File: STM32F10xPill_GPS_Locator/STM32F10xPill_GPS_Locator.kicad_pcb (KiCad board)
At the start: 2 copper layers, 3 parts, among them U1 STM32F100C4Tx, U2 QMC5883P, U4 ATGM336H-5N31

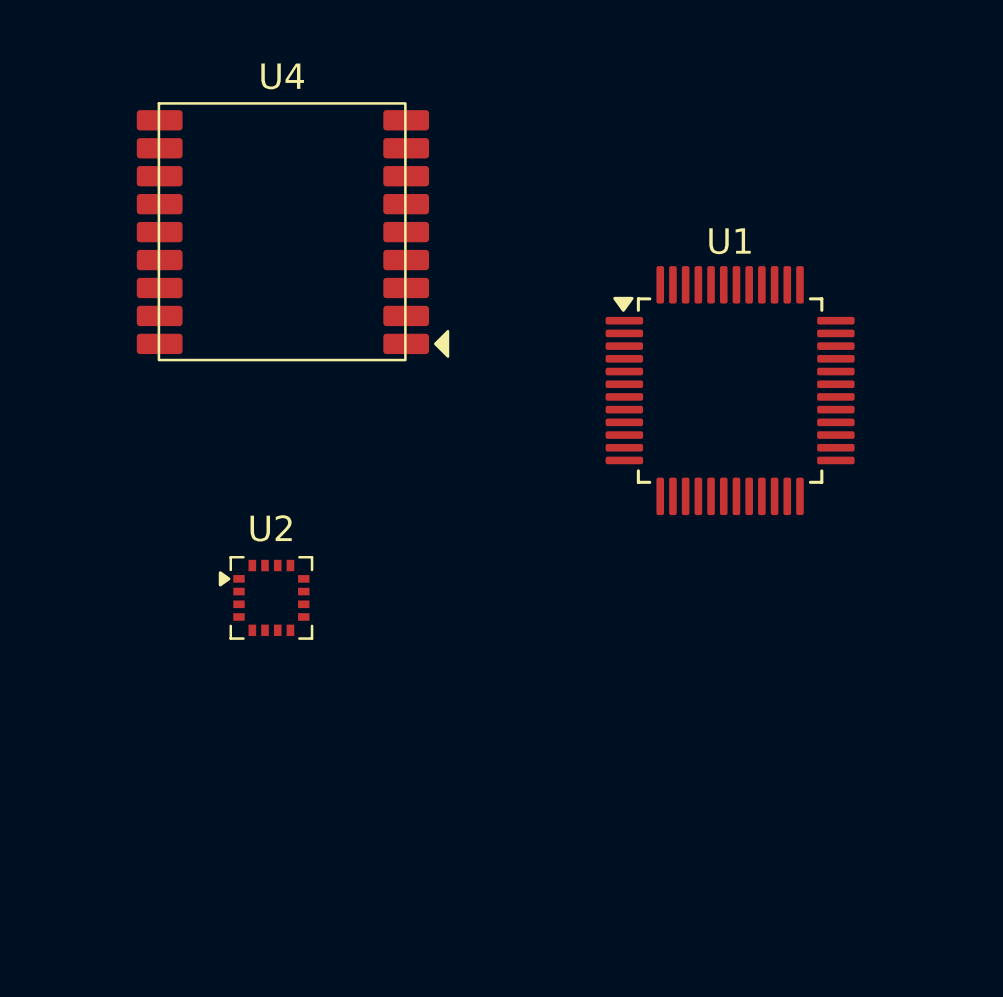
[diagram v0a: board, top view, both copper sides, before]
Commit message: Schematic is largely complete
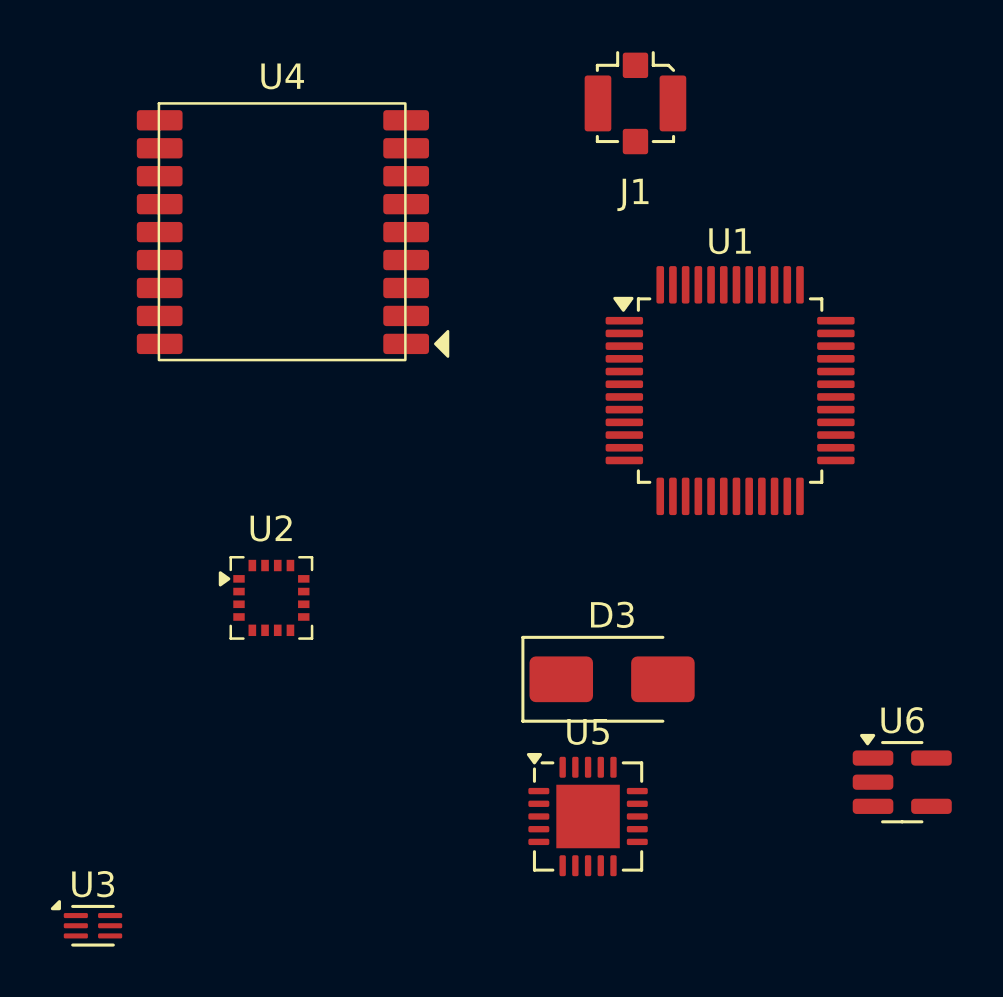
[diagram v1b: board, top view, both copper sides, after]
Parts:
- added D3: SMAJ5.0A, Diode_SMD:D_SMA, F.Cu at (143.6, 98.2)
- added J1: Antenna, Connector_Coaxial:U.FL_Molex_MCRF_73412-0110_Vertical, F.Cu at (144.5, 75.5)
- added U3: AT2659, Package_DFN_QFN:DFN-6_1.6x1.3mm_P0.4mm, F.Cu at (123.2, 107.9)
- added U5: MCP73871T-2CCI/ML, Package_DFN_QFN:QFN-20-1EP_4x4mm_P0.5mm_EP2.5x2.5mm, F.Cu at (142.7, 103.6)
- added U6: TPS61022, Package_TO_SOT_SMD:SC-74A-5_1.55x2.9mm_P0.95mm, F.Cu at (155.0, 102.2)
- U1: value STM32F100C4Tx -> STM32F100C4T6
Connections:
- net +3.3V renamed Net-(JP6-B)
- net +BATT renamed Net-(JP7-B)
- U1 pad 21: unconnected-(U1-PB10-Pad21) -> SCK
- U1 pad 22: unconnected-(U1-PB11-Pad22) -> SDA
- U2 pad 1: unconnected-(U2-SCK-Pad1) -> SCK
- U2 pad 10: unconnected-(U2-C1-Pad10) -> Net-(U2-C1)
- U2 pad 11: unconnected-(U2-GND-Pad11) -> GND
- U2 pad 16: unconnected-(U2-SDA-Pad16) -> SDA
- U2 pad 2: unconnected-(U2-VDD-Pad2) -> Net-(JP5-B)
- U2 pad 9: unconnected-(U2-GND-Pad9) -> GND
- U4 pad 1: unconnected-(U4-GND-Pad1) -> GND
- U4 pad 10: unconnected-(U4-GND-Pad10) -> GND
- U4 pad 11: unconnected-(U4-RF_IN-Pad11) -> Net-(U3-RFOUT)
- U4 pad 12: unconnected-(U4-GND-Pad12) -> GND
- U4 pad 16: unconnected-(U4-SDA-Pad16) -> Net-(U4-SDA)
- U4 pad 17: unconnected-(U4-SCL-Pad17) -> Net-(U4-SCL)
- U4 pad 2: unconnected-(U4-TXD-Pad2) -> GPS_TX
- U4 pad 3: unconnected-(U4-ON/OFF-Pad3) -> GPS_RX
- U4 pad 4: unconnected-(U4-1PPS-Pad4) -> Net-(U4-1PPS)
- U4 pad 6: unconnected-(U4-VBAT-Pad6) -> Net-(JP3-B)
- U4 pad 8: unconnected-(U4-VCC-Pad8) -> Net-(JP4-B)
- U4 pad 9: unconnected-(U4-nRESET-Pad9) -> Net-(U4-nRESET)

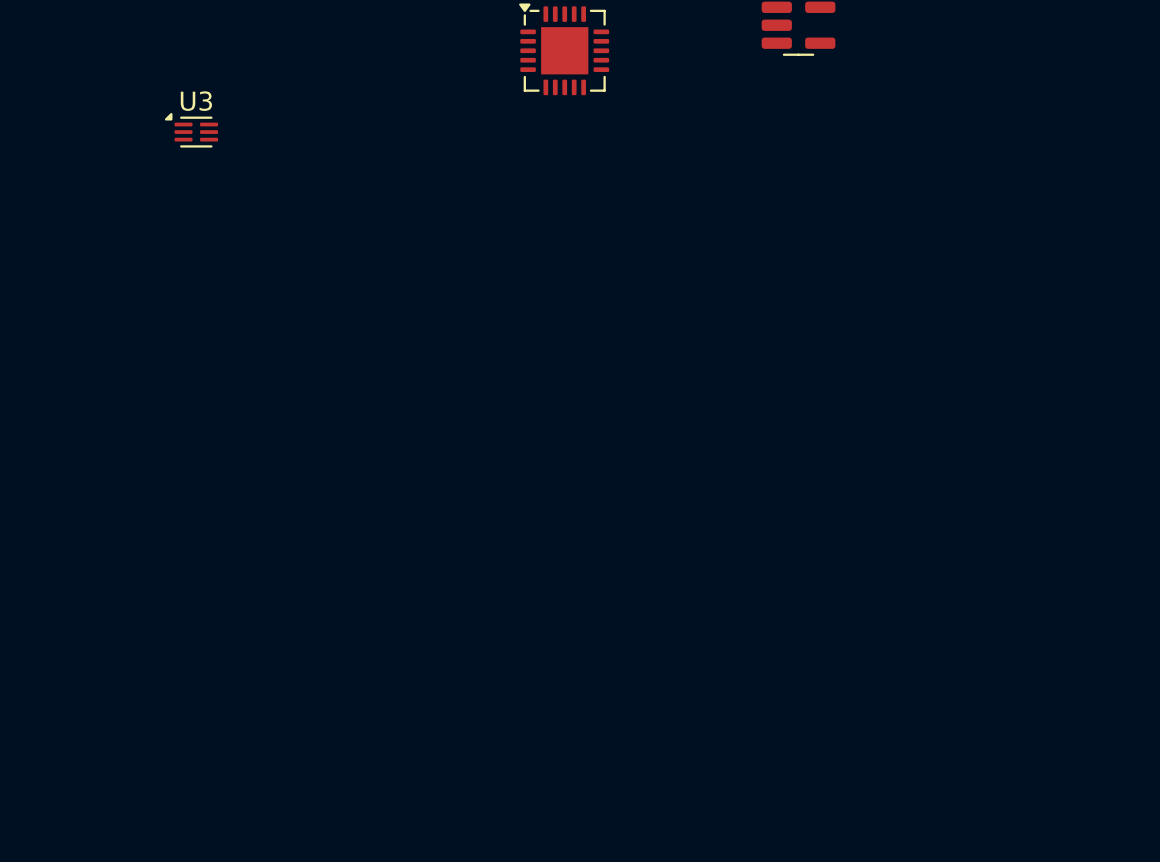
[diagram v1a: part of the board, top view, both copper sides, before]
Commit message: Updated net names, submit schematic for feedback
After feedback is incorporated, PCB layout is ready to begin
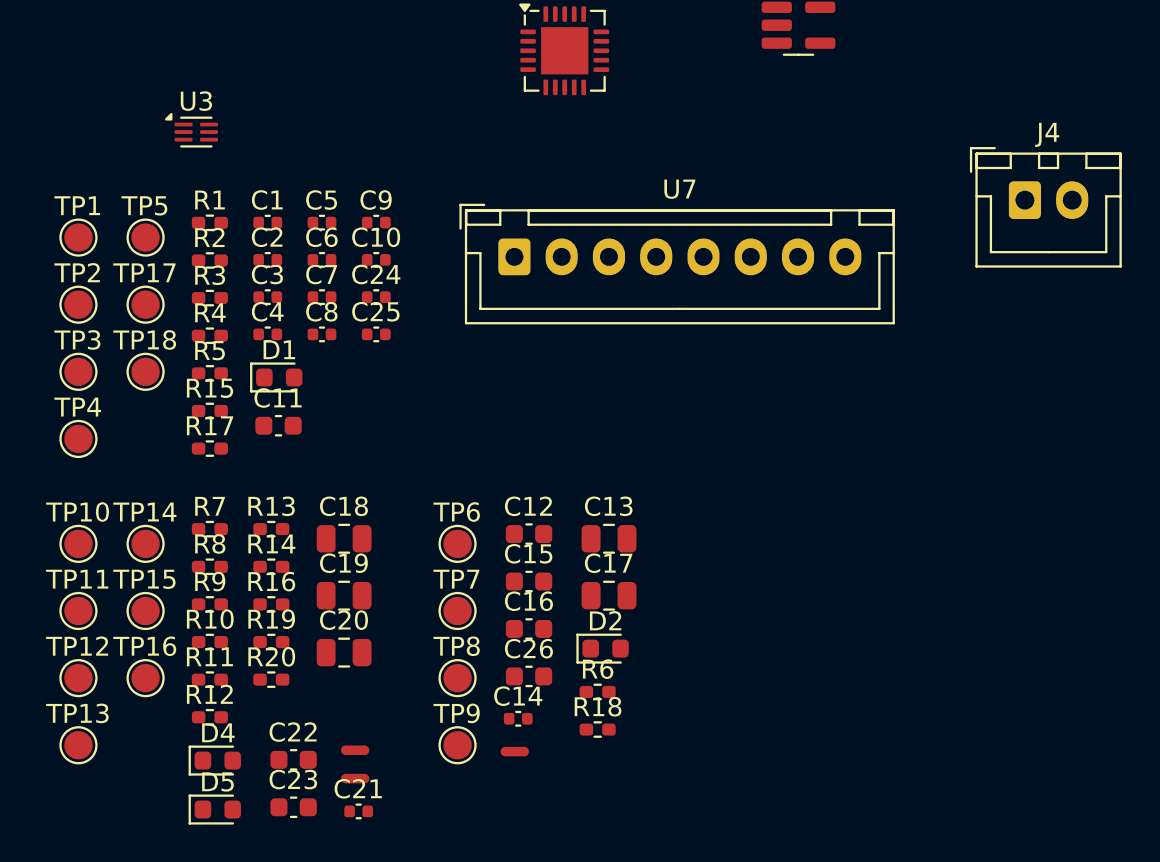
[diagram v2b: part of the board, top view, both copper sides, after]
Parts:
- added C1: 22p, Capacitor_SMD:C_0402_1005Metric, F.Cu at (127.0, 112.7)
- added C10: 22p, Capacitor_SMD:C_0402_1005Metric, F.Cu at (132.7, 114.7)
- added C11: 100n, Capacitor_SMD:C_0603_1608Metric, F.Cu at (127.5, 123.4)
- added C12: 100n, Capacitor_SMD:C_0603_1608Metric, F.Cu at (140.8, 129.2)
- added C13: 4u7, Capacitor_SMD:C_0805_2012Metric, F.Cu at (145.0, 129.4)
- added C14: 470p, Capacitor_SMD:C_0402_1005Metric, F.Cu at (140.2, 138.9)
- added C15: 100n, Capacitor_SMD:C_0603_1608Metric, F.Cu at (140.8, 131.7)
- added C16: 100n, Capacitor_SMD:C_0603_1608Metric, F.Cu at (140.8, 134.2)
- added C17: 10u, Capacitor_SMD:C_0805_2012Metric, F.Cu at (145.0, 132.4)
- added C18: 4u7, Capacitor_SMD:C_0805_2012Metric, F.Cu at (131.0, 129.4)
- added C19: 10u, Capacitor_SMD:C_0805_2012Metric, F.Cu at (131.0, 132.4)
- added C2: 22p, Capacitor_SMD:C_0402_1005Metric, F.Cu at (127.0, 114.7)
- added C20: 2u2, Capacitor_SMD:C_0805_2012Metric, F.Cu at (131.0, 135.4)
- added C21: 1p, Capacitor_SMD:C_0402_1005Metric, F.Cu at (131.8, 143.8)
- added C22: 2u2, Capacitor_SMD:C_0603_1608Metric, F.Cu at (128.3, 141.1)
- added C23: 2u2, Capacitor_SMD:C_0603_1608Metric, F.Cu at (128.3, 143.6)
- added C24: 22p, Capacitor_SMD:C_0402_1005Metric, F.Cu at (132.7, 116.6)
- added C25: 22p, Capacitor_SMD:C_0402_1005Metric, F.Cu at (132.7, 118.6)
- added C26: 100n, Capacitor_SMD:C_0603_1608Metric, F.Cu at (140.8, 136.7)
- added C3: 14p, Capacitor_SMD:C_0402_1005Metric, F.Cu at (127.0, 116.6)
- added C4: 14p, Capacitor_SMD:C_0402_1005Metric, F.Cu at (127.0, 118.6)
- added C5: 100n, Capacitor_SMD:C_0402_1005Metric, F.Cu at (129.8, 112.7)
- added C6: 100n, Capacitor_SMD:C_0402_1005Metric, F.Cu at (129.8, 114.7)
- added C7: 100n, Capacitor_SMD:C_0402_1005Metric, F.Cu at (129.8, 116.6)
- added C8: 100n, Capacitor_SMD:C_0402_1005Metric, F.Cu at (129.8, 118.6)
- added C9: 100n, Capacitor_SMD:C_0402_1005Metric, F.Cu at (132.7, 112.7)
- added D1: RED, LED_SMD:LED_0603_1608Metric, F.Cu at (127.6, 120.9)
- added D2: RED, LED_SMD:LED_0603_1608Metric, F.Cu at (144.8, 135.2)
- added D4: RED, LED_SMD:LED_0603_1608Metric, F.Cu at (124.3, 141.1)
- added D5: RED, LED_SMD:LED_0603_1608Metric, F.Cu at (124.3, 143.7)
- added J4: Conn_01x02, Connector_JST:JST_XH_B2B-XH-A_1x02_P2.50mm_Vertical, F.Cu at (167.0, 111.5)
- added NT1: NetTie_2, NetTie:NetTie-2_SMD_Pad0.5mm, F.Cu at (131.6, 140.6)
- added NT2: NetTie_2, NetTie:NetTie-2_SMD_Pad0.5mm, F.Cu at (131.6, 142.1)
- added NT3: NetTie_2, NetTie:NetTie-2_SMD_Pad0.5mm, F.Cu at (140.0, 140.7)
- added R1: 453 1%, Resistor_SMD:R_0402_1005Metric_Pad0.72x0.64mm_HandSolder, F.Cu at (123.9, 112.7)
- added R10: 330k, Resistor_SMD:R_0402_1005Metric_Pad0.72x0.64mm_HandSolder, F.Cu at (123.9, 134.9)
- added R11: 110k, Resistor_SMD:R_0402_1005Metric_Pad0.72x0.64mm_HandSolder, F.Cu at (123.9, 136.9)
- added R12: 10k, Resistor_SMD:R_0402_1005Metric_Pad0.72x0.64mm_HandSolder, F.Cu at (123.9, 138.8)
- added R13: 453k, Resistor_SMD:R_0402_1005Metric_Pad0.72x0.64mm_HandSolder, F.Cu at (127.1, 128.9)
- added R14: 100k, Resistor_SMD:R_0402_1005Metric_Pad0.72x0.64mm_HandSolder, F.Cu at (127.1, 130.9)
- added R15: 10k, Resistor_SMD:R_0402_1005Metric_Pad0.72x0.64mm_HandSolder, F.Cu at (123.9, 122.7)
- added R16: 10k, Resistor_SMD:R_0402_1005Metric_Pad0.72x0.64mm_HandSolder, F.Cu at (127.1, 132.9)
- added R17: 10k, Resistor_SMD:R_0402_1005Metric_Pad0.72x0.64mm_HandSolder, F.Cu at (123.9, 124.6)
- added R18: 0, Resistor_SMD:R_0402_1005Metric_Pad0.72x0.64mm_HandSolder, F.Cu at (144.4, 139.5)
- added R19: 330, Resistor_SMD:R_0402_1005Metric_Pad0.72x0.64mm_HandSolder, F.Cu at (127.1, 134.9)
- added R2: 10k, Resistor_SMD:R_0402_1005Metric_Pad0.72x0.64mm_HandSolder, F.Cu at (123.9, 114.7)
- added R20: 330, Resistor_SMD:R_0402_1005Metric_Pad0.72x0.64mm_HandSolder, F.Cu at (127.1, 136.9)
- added R3: 510, Resistor_SMD:R_0402_1005Metric_Pad0.72x0.64mm_HandSolder, F.Cu at (123.9, 116.7)
- added R4: 2k7, Resistor_SMD:R_0402_1005Metric_Pad0.72x0.64mm_HandSolder, F.Cu at (123.9, 118.7)
- added R5: 2k7, Resistor_SMD:R_0402_1005Metric_Pad0.72x0.64mm_HandSolder, F.Cu at (123.9, 120.7)
- added R6: 5k1, Resistor_SMD:R_0402_1005Metric_Pad0.72x0.64mm_HandSolder, F.Cu at (144.4, 137.5)
- added R7: 10k, Resistor_SMD:R_0402_1005Metric_Pad0.72x0.64mm_HandSolder, F.Cu at (123.9, 128.9)
- added R8: 2k2, Resistor_SMD:R_0402_1005Metric_Pad0.72x0.64mm_HandSolder, F.Cu at (123.9, 130.9)
- added R9: 10k, Resistor_SMD:R_0402_1005Metric_Pad0.72x0.64mm_HandSolder, F.Cu at (123.9, 132.9)
- added TP1: nRST, TestPoint:TestPoint_Pad_D1.5mm, F.Cu at (116.9, 113.5)
- added TP10: REG_OUT, TestPoint:TestPoint_Pad_D1.5mm, F.Cu at (116.9, 129.7)
- added TP11: REG_SW, TestPoint:TestPoint_Pad_D1.5mm, F.Cu at (116.9, 133.2)
- added TP12: REG_FB, TestPoint:TestPoint_Pad_D1.5mm, F.Cu at (116.9, 136.8)
- added TP13: PPM_BATT, TestPoint:TestPoint_Pad_D1.5mm, F.Cu at (116.9, 140.3)
- added TP14: PPM_VPCC, TestPoint:TestPoint_Pad_D1.5mm, F.Cu at (120.5, 129.7)
- added TP15: PPM_IN, TestPoint:TestPoint_Pad_D1.5mm, F.Cu at (120.5, 133.2)
- added TP16: PPM_OUT, TestPoint:TestPoint_Pad_D1.5mm, F.Cu at (120.5, 136.8)
- added TP17: SCK, TestPoint:TestPoint_Pad_D1.5mm, F.Cu at (120.5, 117.0)
- added TP18: SDA, TestPoint:TestPoint_Pad_D1.5mm, F.Cu at (120.5, 120.6)
- added TP2: MCU_OSCIN, TestPoint:TestPoint_Pad_D1.5mm, F.Cu at (116.9, 117.0)
- added TP3: MCU_OSCOUT, TestPoint:TestPoint_Pad_D1.5mm, F.Cu at (116.9, 120.6)
- added TP4: RTC_OSCIN, TestPoint:TestPoint_Pad_D1.5mm, F.Cu at (116.9, 124.1)
- added TP5: RTC_OSCOUT, TestPoint:TestPoint_Pad_D1.5mm, F.Cu at (120.5, 113.5)
- added TP6: GPS_1PPS, TestPoint:TestPoint_Pad_D1.5mm, F.Cu at (137.0, 129.7)
- added TP7: GPS_SDA, TestPoint:TestPoint_Pad_D1.5mm, F.Cu at (137.0, 133.2)
- added TP8: GPS_SCL, TestPoint:TestPoint_Pad_D1.5mm, F.Cu at (137.0, 136.8)
- added TP9: GPS_nRESET, TestPoint:TestPoint_Pad_D1.5mm, F.Cu at (137.0, 140.3)
- added U7: ~, Connector_JST:JST_XH_B8B-XH-A_1x08_P2.50mm_Vertical, F.Cu at (140.0, 114.5)
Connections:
- net Net-(BT1-+) renamed /Power Supply/PPM_BATT
- net Net-(JP8-A) renamed /Power Supply/PPM_OUT
- net Net-(U3-RFIN) renamed /Peripherals/LNA_RFIN
- D3 pad 1: Net-(D3-A1) -> /Power Supply/5V_IN
- J1 pad 1: Net-(J1-In) -> /Peripherals/ANT_IN
- U1 pad 18: unconnected-(U1-PB0-Pad18) -> BATT_CHARGING
- U1 pad 19: unconnected-(U1-PB1-Pad19) -> BATT_LOW
- U1 pad 25: unconnected-(U1-PB12-Pad25) -> LCD_DC
- U1 pad 26: unconnected-(U1-PB13-Pad26) -> LCD_RST
- U1 pad 27: unconnected-(U1-PB14-Pad27) -> /Controller/BUTTON_A
- U1 pad 28: unconnected-(U1-PB15-Pad28) -> /Controller/BUTTON_B
- U1 pad 38: unconnected-(U1-PA15-Pad38) -> LCD_CE
- U1 pad 39: unconnected-(U1-PB3-Pad39) -> LCD_CLK
- U1 pad 41: unconnected-(U1-PB5-Pad41) -> LCD_MOSI
- U1 pad 42: unconnected-(U1-PB6-Pad42) -> GPS_RX
- U1 pad 43: unconnected-(U1-PB7-Pad43) -> GPS_TX
- U1 pad 45: unconnected-(U1-PB8-Pad45) -> LCD_BL
- U2 pad 10: Net-(U2-C1) -> /Peripherals/QMC_RESCAP
- U2 pad 2: Net-(JP5-B) -> /Peripherals/QMC_VDD
- U3 pad 4: Net-(JP2-B) -> /Peripherals/LNA_VCC
- U3 pad 6: Net-(U3-RFOUT) -> /Peripherals/LNA_RFOUT
- U4 pad 11: Net-(U3-RFOUT) -> /Peripherals/GPS_RFIN
- U4 pad 3: GPS_RX -> /Peripherals/GPS_ONOFF
- U4 pad 4: Net-(U4-1PPS) -> /Peripherals/GPS_1PPS
- U4 pad 6: Net-(JP3-B) -> /Peripherals/GPS_VBATT
- U4 pad 8: Net-(JP4-B) -> /Peripherals/GPS_VCC
- U5 pad 12: Net-(U5-PROG3) -> /Power Supply/PPM_PROG3
- U5 pad 13: Net-(U5-PROG1) -> /Power Supply/PPM_PROG1
- U5 pad 18: Net-(D3-A1) -> /Power Supply/PPM_IN
- U5 pad 19: Net-(D3-A1) -> /Power Supply/PPM_IN
- U5 pad 2: Net-(U5-VPCC) -> /Power Supply/PPM_VPCC
- U5 pad 5: Net-(U5-THERM) -> /Power Supply/PPM_THERM
- U6 pad 2: Net-(U6-SW) -> /Power Supply/REG_SW2
- U6 pad 3: Net-(SW2-A) -> +BATT
- U6 pad 4: Net-(U6-FB) -> /Power Supply/REG_FB
- U6 pad 5: Net-(JP8-B) -> /Power Supply/REG_IN

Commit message: Add all footprints and symbols, retouch schametic
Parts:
- added BT1: Single LiPo, Battery:BatteryHolder_MPD_BH-18650-PC2, F.Cu at (95.5, 157.0)
- added C23: 2u2, Capacitor_SMD:C_0603_1608Metric, F.Cu at (105.9, 138.6)
- added J2: Conn_01x03, Connector_PinHeader_2.54mm:PinHeader_1x03_P2.54mm_Vertical, F.Cu at (113.5, 94.0)
- added J3: Conn_01x05, Connector_PinHeader_2.54mm:PinHeader_1x05_P2.54mm_Vertical, F.Cu at (96.0, 115.3)
- added JP1: GPS_On-Off, Jumper:SolderJumper-3_P1.3mm_Open_Pad1.0x1.5mm_NumberLabels, F.Cu at (107.5, 114.7)
- added JP2: Jumper_2_Open, Jumper:SolderJumper-2_P1.3mm_Open_Pad1.0x1.5mm, F.Cu at (102.5, 114.7)
- added JP3: Jumper_2_Open, Jumper:SolderJumper-2_P1.3mm_Open_Pad1.0x1.5mm, F.Cu at (102.5, 118.3)
- added JP4: Jumper_2_Open, Jumper:SolderJumper-2_P1.3mm_Open_Pad1.0x1.5mm, F.Cu at (102.5, 121.8)
- added JP5: Jumper_2_Open, Jumper:SolderJumper-2_P1.3mm_Open_Pad1.0x1.5mm, F.Cu at (102.5, 125.4)
- added JP6: Jumper_2_Open, Jumper:SolderJumper-2_P1.3mm_Open_Pad1.0x1.5mm, F.Cu at (95.9, 129.5)
- added JP8: Jumper_2_Open, Jumper:SolderJumper-2_P1.3mm_Open_Pad1.0x1.5mm, F.Cu at (106.1, 135.5)
- added L1: 6n8, Inductor_SMD:L_0603_1608Metric, F.Cu at (148.7, 140.4)
- added L2: 1u, Inductor_SMD:L_1008_2520Metric, F.Cu at (167.4, 120.0)
- added NT4: NetTie_2, NetTie:NetTie-2_SMD_Pad0.5mm, F.Cu at (109.5, 134.5)
- added NT5: NetTie_2, NetTie:NetTie-2_SMD_Pad0.5mm, F.Cu at (109.5, 136.0)
- added Q1: 2301D, Package_TO_SOT_SMD:SOT-23, F.Cu at (106.3, 131.5)
- added R21: 10k, Resistor_SMD:R_0402_1005Metric_Pad0.72x0.64mm_HandSolder, F.Cu at (102.0, 137.2)
- added R22: 330, Resistor_SMD:R_0402_1005Metric_Pad0.72x0.64mm_HandSolder, F.Cu at (102.0, 139.2)
- added R23: 10k, Resistor_SMD:R_0402_1005Metric_Pad0.72x0.64mm_HandSolder, F.Cu at (164.9, 135.5)
- added SW1: TS-1092S-B3D2-G, Button_Switch_SMD:SW_Tactile_SPST_NO_Straight_CK_PTS636Sx25SMTRLFS, F.Cu at (88.4, 115.6)
- added SW2: Power, Connector_JST:JST_XH_B2B-XH-A_1x02_P2.50mm_Vertical, F.Cu at (157.3, 133.4)
- added SW3: TS-1092S-B3D2-G, Button_Switch_SMD:SW_Tactile_SPST_NO_Straight_CK_PTS636Sx25SMTRLFS, F.Cu at (88.4, 120.8)
- added SW4: TS-1092S-B3D2-G, Button_Switch_SMD:SW_Tactile_SPST_NO_Straight_CK_PTS636Sx25SMTRLFS, F.Cu at (88.4, 126.1)
- added TP19: 3V3_SW_GATE, TestPoint:TestPoint_Pad_D1.5mm, F.Cu at (102.1, 130.9)
- added TP20: 3V3_SW, TestPoint:TestPoint_Pad_D1.5mm, F.Cu at (102.1, 134.5)
- added Y1: 16MHz, Crystal:Crystal_SMD_3225-4Pin_3.2x2.5mm, F.Cu at (165.9, 132.3)
- added Y2: 32.768kHz, Crystal:Crystal_SMD_HC49-SD, F.Cu at (161.2, 126.9)
- J1: value Antenna -> 734120110
- U3: value AT2659 -> AT2659S; footprint Package_DFN_QFN:DFN-6_1.6x1.3mm_P0.4mm -> Package_TO_SOT_SMD:SOT-23-6
- moved U3 2.63 mm to (124.4, 105.5)
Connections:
- C11 pad 2: Net-(JP7-B) -> Net-(JP6-B)
- C21 pad 2: +BATT -> +3.3V
- C22 pad 2: +BATT -> +3.3V
- R13 pad 2: +BATT -> +3.3V
- TP10 pad 1: +BATT -> +3.3V
- U1 pad 1: Net-(JP7-B) -> Net-(JP6-B)
- U1 pad 31: unconnected-(U1-PA10-Pad31) -> Net-(SW2-A)
- U6 pad 3: +BATT -> +3.3V

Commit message: Begin PCB layout
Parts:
- removed SW1: TS-1092S-B3D2-G, Button_Switch_SMD:SW_Tactile_SPST_NO_Straight_CK_PTS636Sx25SMTRLFS
- removed the TP2 at (116.9, 117.0)
- removed the TP3 at (116.9, 120.6)
- removed TP4: RTC_OSCIN, TestPoint:TestPoint_Pad_D1.5mm
- removed TP5: RTC_OSCOUT, TestPoint:TestPoint_Pad_D1.5mm
- removed the U7 at (140.0, 114.5)
- added C27: 22p, Capacitor_SMD:C_0402_1005Metric, F.Cu at (136.0, 102.6)
- added H1: MountingHole, MountingHole:MountingHole_2.2mm_M2, F.Cu at (160.0, 40.5)
- added H2: MountingHole, MountingHole:MountingHole_2.2mm_M2, F.Cu at (223.0, 40.5)
- added H3: MountingHole, MountingHole:MountingHole_2.2mm_M2, F.Cu at (223.0, 124.5)
- added H4: MountingHole, MountingHole:MountingHole_2.2mm_M2, F.Cu at (160.0, 124.5)
- added R24: 10k, Resistor_SMD:R_0402_1005Metric_Pad0.72x0.64mm_HandSolder, F.Cu at (133.0, 102.6)
- added SW5: TS-1092S-B3D2-G, Button_Switch_SMD:SW_Tactile_SPST_NO_Straight_CK_PTS636Sx25SMTRLFS, F.Cu at (191.5, 107.5)
- added SW6: PTS645VH58-2 LFS, Button_Switch_THT:SW_Tactile_SPST_Angled_PTS645Vx58-2LFS, B.Cu at (162.2, 78.2)
- added U4: ~, Connector_PinSocket_2.54mm:PinSocket_1x08_P2.54mm_Vertical, F.Cu at (182.6, 42.5)
- BT1: moved to B.Cu
- J1: renamed from J2; footprint Connector_PinHeader_2.54mm:PinHeader_1x03_P2.54mm_Vertical -> Connector_PinHeader_2.54mm:PinHeader_1x03_P2.54mm_Horizontal; moved to B.Cu
- J2: renamed from J3; footprint Connector_PinHeader_2.54mm:PinHeader_1x05_P2.54mm_Vertical -> Connector_PinHeader_2.54mm:PinHeader_1x05_P2.54mm_Horizontal; moved to B.Cu
- J3: renamed from J4; footprint Connector_JST:JST_XH_B2B-XH-A_1x02_P2.50mm_Vertical -> Connector_JST:JST_PH_B2B-PH-K_1x02_P2.00mm_Vertical; moved to B.Cu
- SW4: renamed from SW2; footprint Connector_JST:JST_XH_B2B-XH-A_1x02_P2.50mm_Vertical -> Connector_JST:JST_PH_B2B-PH-K_1x02_P2.00mm_Vertical; moved to B.Cu
- Y2: footprint Crystal:Crystal_SMD_HC49-SD -> Crystal:Crystal_SMD_3215-2Pin_3.2x1.5mm
- moved JP3 245.3 mm to (343.9, 81.5)
- moved JP4 240.1 mm to (328.2, 32.8)
- moved JP5 240.1 mm to (333.2, 32.8)
- moved JP6 240.1 mm to (328.2, 36.4)
- moved JP7 240.1 mm to (328.2, 39.9)
- moved U7 228.8 mm to (355.0, 36.0), turned to 90 degrees
- moved U6 227.6 mm to (340.2, 33.4)
- moved C23 222.0 mm to (328.1, 46.8)
- moved NT1 221.1 mm to (352.3, 155.2)
- moved NT2 221.1 mm to (352.3, 153.7)
- moved R10 221.1 mm to (344.6, 148.0)
- moved R11 221.1 mm to (344.6, 150.0)
- moved R12 221.1 mm to (344.6, 152.0)
- moved R13 221.1 mm to (347.8, 146.0)
- moved R14 221.1 mm to (347.8, 148.0)
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- renumbered C7 to C10, C8 to C11, C9 to C12, C5 to C13, C19 to C14, C18 to C15, C20 to C16, C21 to C17, C22 to C18, C23 to C19, C26 to C20, C12 to C21, C13 to C22, C14 to C23, C15 to C24, C16 to C25, C17 to C26, C10 to C5, C25 to C6, C24 to C7, C11 to C8, C6 to C9, D3 to D2, D5 to D3, D2 to D5, J1 to J4, JP6 to JP1, JP8 to JP2, JP5 to JP3, JP2 to JP4, JP1 to JP5, JP3 to JP6, JP4 to JP7, L2 to L1, L1 to L2, NT2 to NT1, NT1 to NT2, NT4 to NT3, NT5 to NT4, NT3 to NT5, R5 to R1, R16 to R13, R19 to R14, R9 to R15, R8 to R16, R7 to R17, R13 to R18, R14 to R19, R4 to R2, R21 to R20, R22 to R21, R18 to R22, R6 to R23, R15 to R3, R17 to R4, R1 to R5, R2 to R6, R3 to R7, R23 to R8, R20 to R9, SW3 to SW2, SW4 to SW3, TP17 to TP1, TP16 to TP10, TP13 to TP11, TP11 to TP12, TP12 to TP13, TP10 to TP14, TP19 to TP15, TP20 to TP16, TP9 to TP17, TP7 to TP18, TP8 to TP19, TP18 to TP2, TP6 to TP20, TP1 to TP3, TP15 to TP8, TP14 to TP9, U5 to U2, U6 to U3, U2 to U5, U3 to U6, U4 to U7
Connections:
- net Net-(JP6-B) renamed /Controller/MCU_VDD
- C7 pad 2: /Controller/BUTTON_B -> /Controller/BUTTON_C
- R4 pad 1: /Controller/BUTTON_B -> /Controller/BUTTON_C
- R8 pad 2: Net-(SW2-A) -> /Controller/POWER_SWITCH
- SW3 pad 2: /Controller/BUTTON_B -> /Controller/BUTTON_C
- SW4 pad 1: Net-(SW2-A) -> /Controller/POWER_SWITCH
- U1 pad 10: unconnected-(U1-PA0-Pad10) -> /Controller/POWER_SWITCH
- U1 pad 28: /Controller/BUTTON_B -> /Controller/BUTTON_C
- U1 pad 31: Net-(SW2-A) -> /Controller/BUTTON_B
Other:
- board outline added: 70 x 91 mm
